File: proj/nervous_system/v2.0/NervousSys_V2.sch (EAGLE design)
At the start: 101 parts, among them IC2 PCA9615DP, IC3 PCA9615DP, IC4 PCA9615DP, IC5 PCA9615DP, IC6 PCA9615DP, IC7 PCA9615DP, IC8 PCA9615DP, IC9 PCA9615DP, J2 54602-908LF, J3 54602-908LF, J4 54602-908LF, J5 54602-908LF, J6 54602-908LF, J7 54602-908LF, J8 54602-908LF, J9 54602-908LF, T1 R-78E5.0-1.0, U1 TCA9548APWRPW24-M

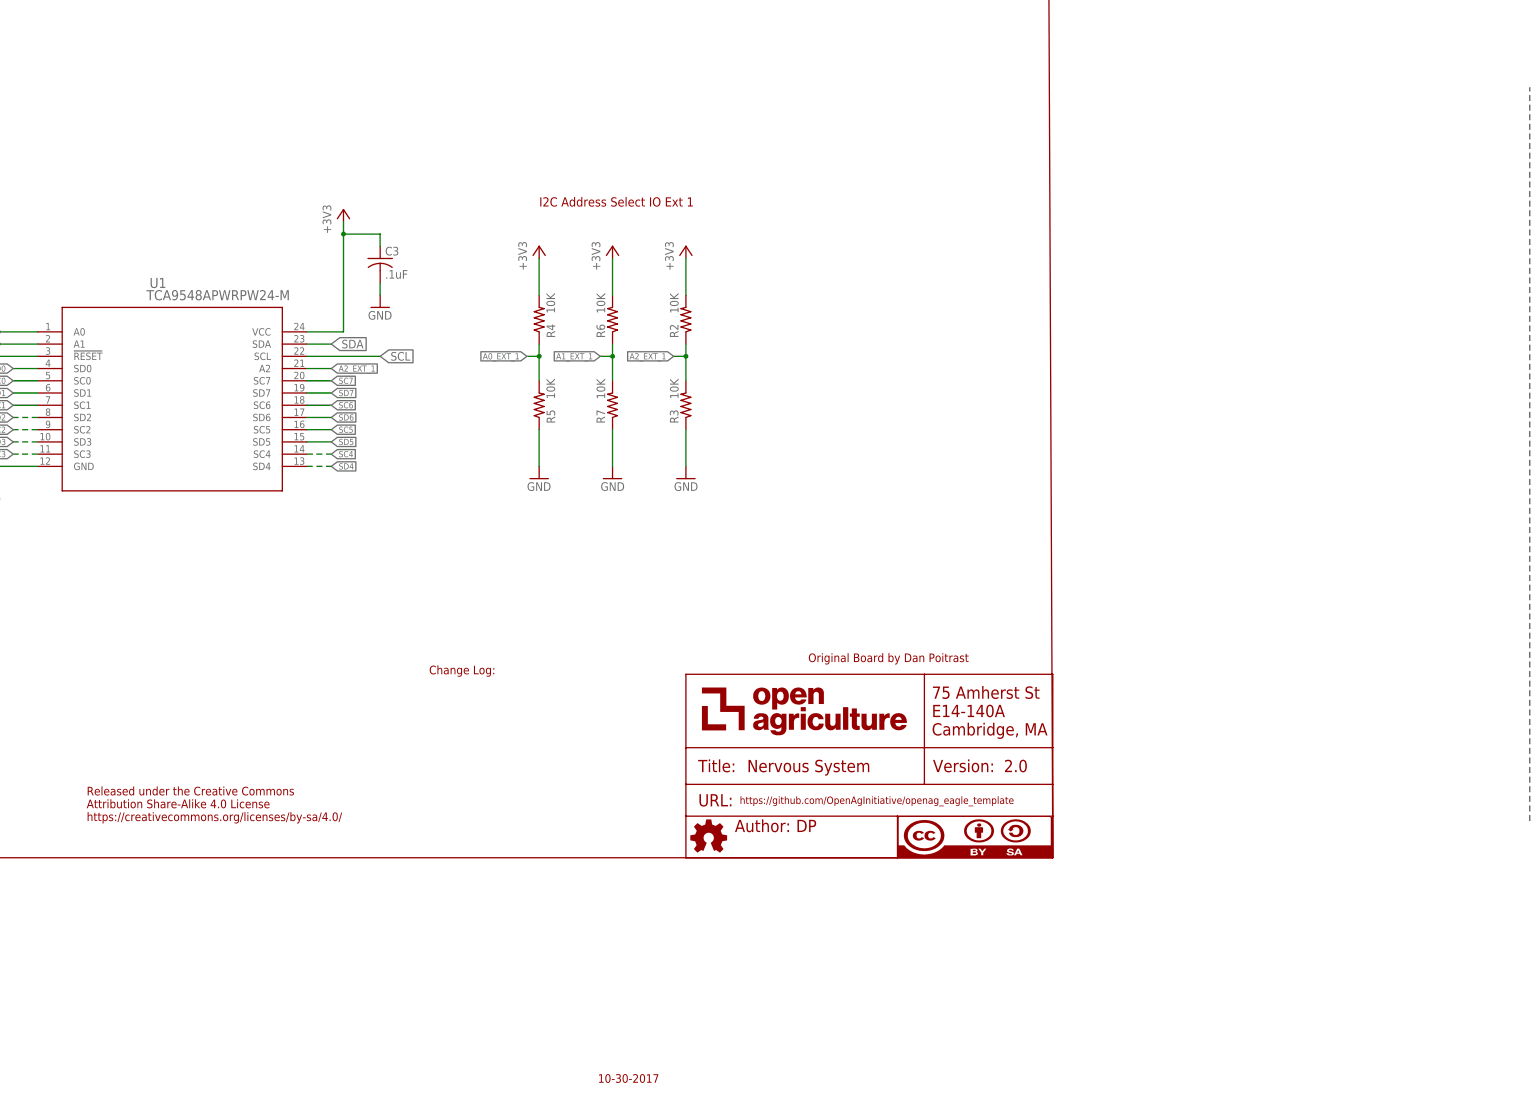
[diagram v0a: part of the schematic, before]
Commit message: NS V2 Layout Change
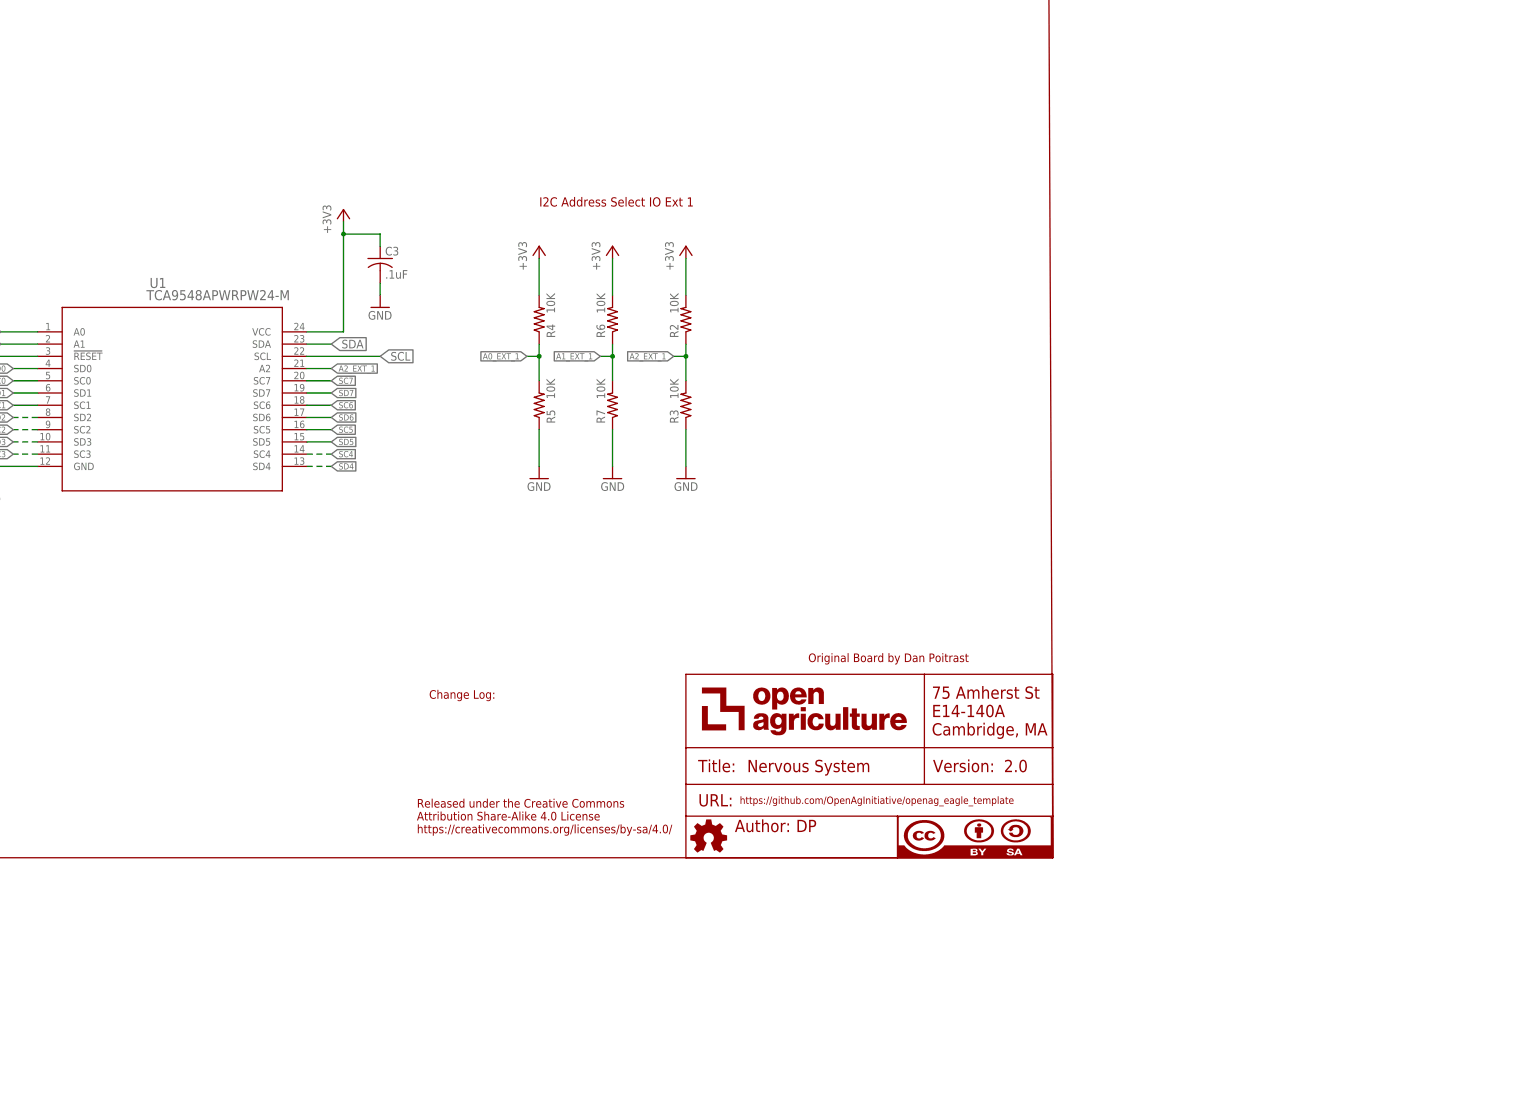
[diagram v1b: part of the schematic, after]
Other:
- note removed: "10-30-2017"
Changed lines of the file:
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@@
 <sheet>
 <plain>
-<text x="-94.488" y="-49.276" size="1.778" layer="94">10-30-2017</text>
 <text x="-50.8" y="38.1" size="1.778" layer="94">Original Board by Dan Poitrast</text>
-<text x="-129.54" y="35.56" size="1.778" layer="94">Change Log:
+<text x="-129.54" y="30.48" size="1.778" layer="94">Change Log:
 </text>
 <text x="-284.48" y="124.46" size="1.905" layer="94" align="top-left">I2C Pull-up Resistors</text>
@@
 <text x="-191.77" y="233.68" size="7.62" layer="103">Power Features</text>
 <text x="-199.39" y="142.24" size="7.62" layer="103">I2C Multiplexer</text>
-<text x="-200.66" y="5.08" size="1.778" layer="94">Released under the Creative Commons
+<text x="-132.08" y="2.54" size="1.778" layer="94">Released under the Creative Commons
 Attribution Share-Alike 4.0 License
 https://creativecommons.org/licenses/by-sa/4.0/</text>
-<wire x1="99.06" y1="5.08" x2="99.06" y2="157.48" width="0.254" layer="97" style="longdash"/>
 <text x="-106.68" y="134.62" size="1.905" layer="94" align="top-left">I2C Address Select IO Ext 1</text>
 <wire x1="-647.7" y1="541.02" x2="-480.06" y2="541.02" width="0.1524" layer="103" style="longdash"/>

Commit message: NSV2
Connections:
- net +3V3: no longer IC2.VDD_(B), IC3.VDD_(B), IC4.VDD_(B), IC5.VDD_(B), IC6.VDD_(B), IC7.VDD_(B), IC8.VDD_(B), IC9.VDD_(B), R18.1, R19.2, R26.1, R27.2, R34.1, R35.2, R42.1, R43.2, R50.1, R51.2, R58.1, R59.2, R66.1, R67.2, R74.1, R75.2
- net +5V: now also IC2.VDD_(B), IC3.VDD_(B), IC4.VDD_(B), IC5.VDD_(B), IC6.VDD_(B), IC7.VDD_(B), IC8.VDD_(B), IC9.VDD_(B), R18.1, R19.2, R26.1, R27.2, R34.1, R35.2, R42.1, R43.2, R50.1, R51.2, R58.1, R59.2, R66.1, R67.2, R74.1, R75.2

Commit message: NSV2.0 Brd Update
Photon header, indicator leds etc
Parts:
- added C2: 0.1uF, openag-capacitors:0.1UF-C0603C104K5RACTU
- added C4: 4.7uF, openag-capacitors:4.7UF-CL21A475KBQNNNE
- added D2, D3, D4: APT1608CGCK, openag-diodes:APT1608CGCK
- added J1: 87583-2010BLF, openag-connectors:87583-2010BLF
- added R10, R11, R12: 100 OHM, openag-resistors:100OHM-RC0603JR-07100RL
- added R86, R87, R88: 0 OHM, openag-resistors:0OHM-RC0603JR-070RL
- added U2: PHOTONH, openag-microcontrollers:PHOTONHPHOTONH
- ATTRIBUTES: URL (none) -> https://github.com/OpenAgInitiative/
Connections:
- new net N$12: D2.A, R10.1
- new net N$2: D3.A, R11.1
- new net N$4: D4.A, R12.1
- new net N$9: C2.1, C4.1, R88.1, U2.3V3
- new net PHOTON_A0: U2.A0
- new net PHOTON_A1: U2.A1
- new net PHOTON_D2: U2.D2
- new net PHOTON_D3: U2.D3
- new net PHOTON_D4: U2.D4
- new net PHOTON_RX: U2.RX
- new net PHOTON_SCL: R87.1, U2.D1
- new net PHOTON_SDA: R86.1, U2.D0
- new net PHOTON_TX: U2.TX
- net +24V: now also R12.2
- net +3V3: now also R10.2, R88.2
- net +5V: now also R11.2
- net GND: now also C2.2, C4.2, D2.C, D3.C, D4.C, J1.1, U2.GND@2, U2.GND@21
- net SCL: now also R87.2
- net SDA: now also R86.2
- net USBM1: now also J1.3
- net USBP1: now also J1.2
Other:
- note added: "24V Indicator LED"
- note added: "3.3V Indicator LED"
- note added: "5V Indicator LED"
- note added: "Indicator LEDs"
- note added: "Photon Microcontroller"
- moved on the sheet: C1, C11, C9, D1, F11, F12, T1

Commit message: USB
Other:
- note added: "USB header"
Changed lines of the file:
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@@
 <wire x1="-25.4" y1="312.42" x2="-96.52" y2="312.42" width="0.1524" layer="103" style="longdash"/>
 <wire x1="-96.52" y1="312.42" x2="-96.52" y2="434.34" width="0.1524" layer="103" style="longdash"/>
+<text x="-368.3" y="530.86" size="5.08" layer="103">USB header</text>
 </plain>
 <instances>
